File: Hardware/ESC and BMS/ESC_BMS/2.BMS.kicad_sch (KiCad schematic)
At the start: 37 parts, among them Q301 SQJ141ELP, Q302 SQJ141ELP, Q303 SQJ141ELP, Q304 SQJ412EP, Q305 SQJ141ELP, SW301 SW_SPST, U301 BQ2057W, U302 BQ2969T

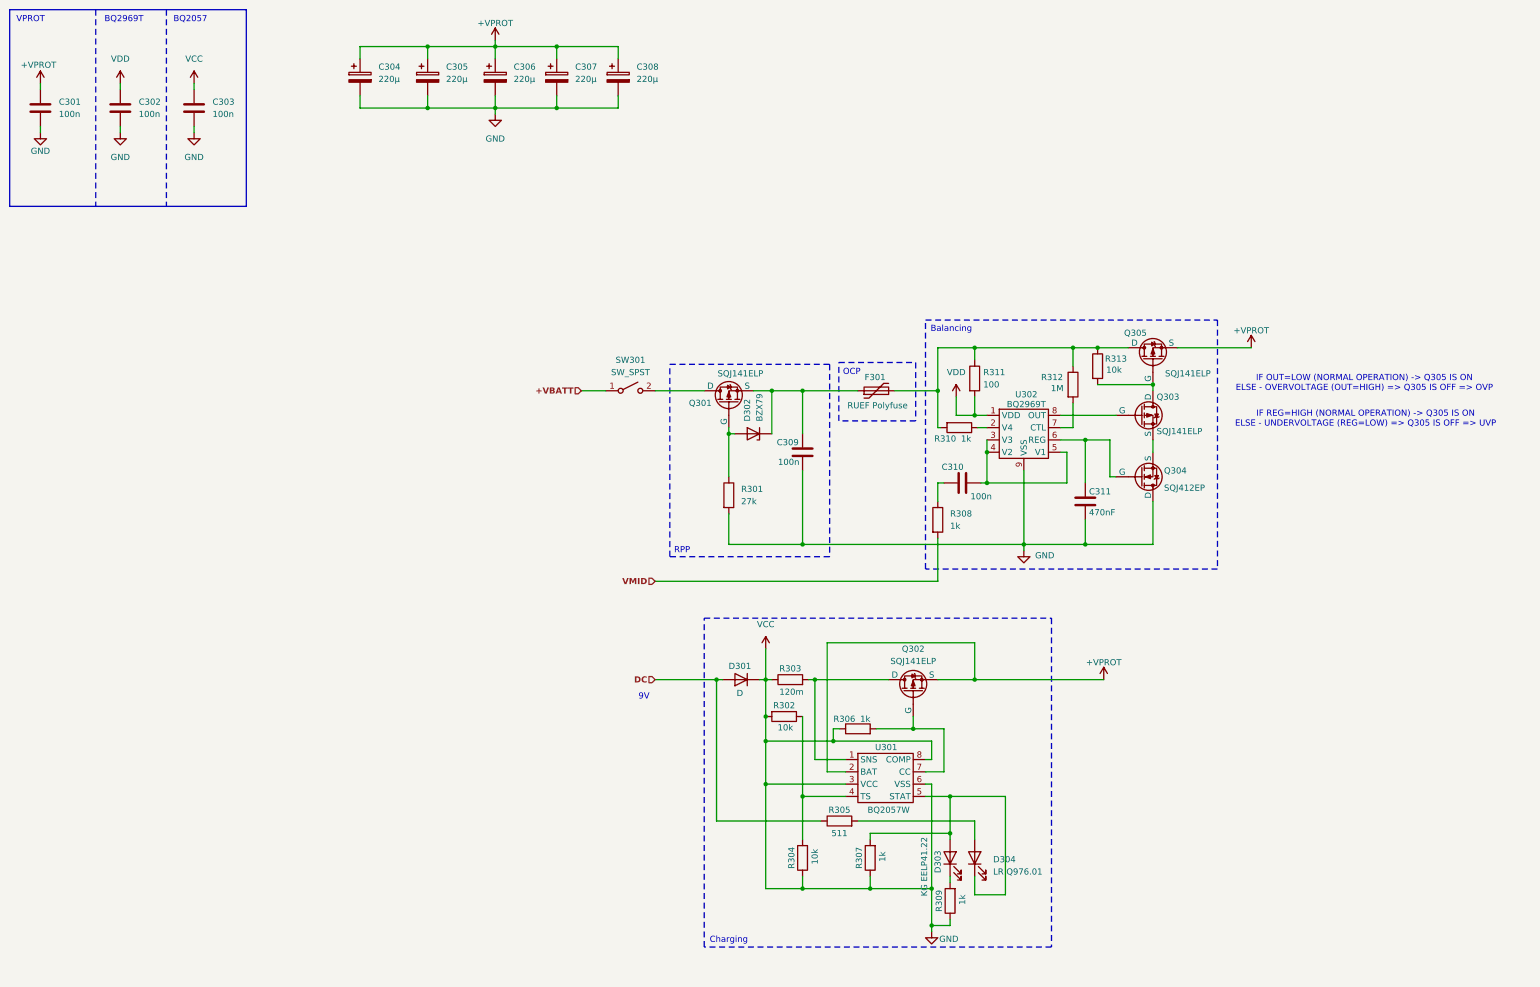
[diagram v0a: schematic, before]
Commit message: footprints almost done and LEDs for charger fixed
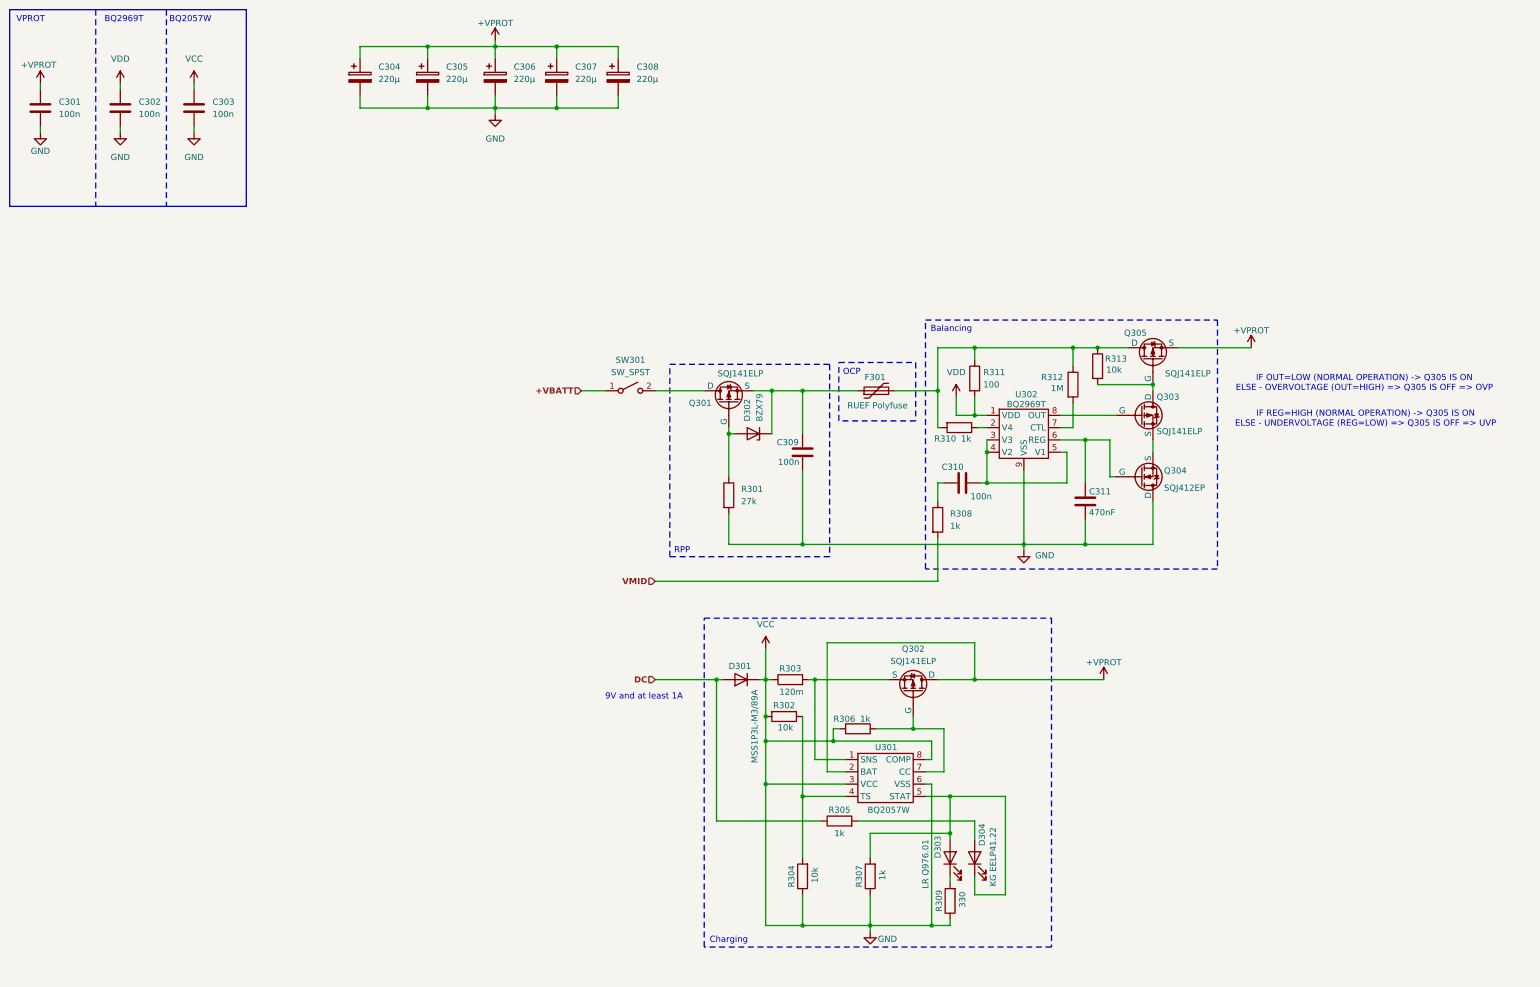
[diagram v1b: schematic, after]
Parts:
- D301: value D -> MSS1P3L-M3/89A
- D303: renamed from D304; footprint https://docs.rs-online.com/01aa/A700000010723894.pdf -> Diode_SMD:D_0603_1608Metric_Pad1.05x0.95mm_HandSolder
- D304: renamed from D303; footprint https://docs.rs-online.com/e1fe/A700000013302439.pdf -> Diode_SMD:D_0603_1608Metric_Pad1.05x0.95mm_HandSolder
- R305: value 511 -> 1k; footprint (none) -> Resistor_SMD:R_0603_1608Metric
- R306, R307, R308, R310, R311: footprint (none) -> Resistor_SMD:R_0603_1608Metric
- R309: value 1k -> 330; footprint (none) -> Resistor_SMD:R_0603_1608Metric
- R312: footprint (none) -> Resistor_SMD:R_0805_2012Metric_Pad1.20x1.40mm_HandSolder
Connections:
- net +VPROT: now also Q302.1 (D); no longer Q302.3 (S)
- net at R309.2: now also D303.1 (K); no longer D304.1 (K)
- net at R307.2, U301.5 (STAT): now also D303.2 (A), D304.1 (K); no longer D303.1 (K), D304.2 (A)
- net at R305.2: now also D304.2 (A); no longer D303.2 (A)
- net at R303.2, U301.1 (SNS): now also Q302.3 (S); no longer Q302.1 (D)
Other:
- note added: "9V and at least 1A"
- note added: "BQ2057W"
- note removed: "9V"
- note removed: "BQ2057"
- moved on the sheet: D303, D304, Q302, R304, R307

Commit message: ESC/BMS fully ready for PCB
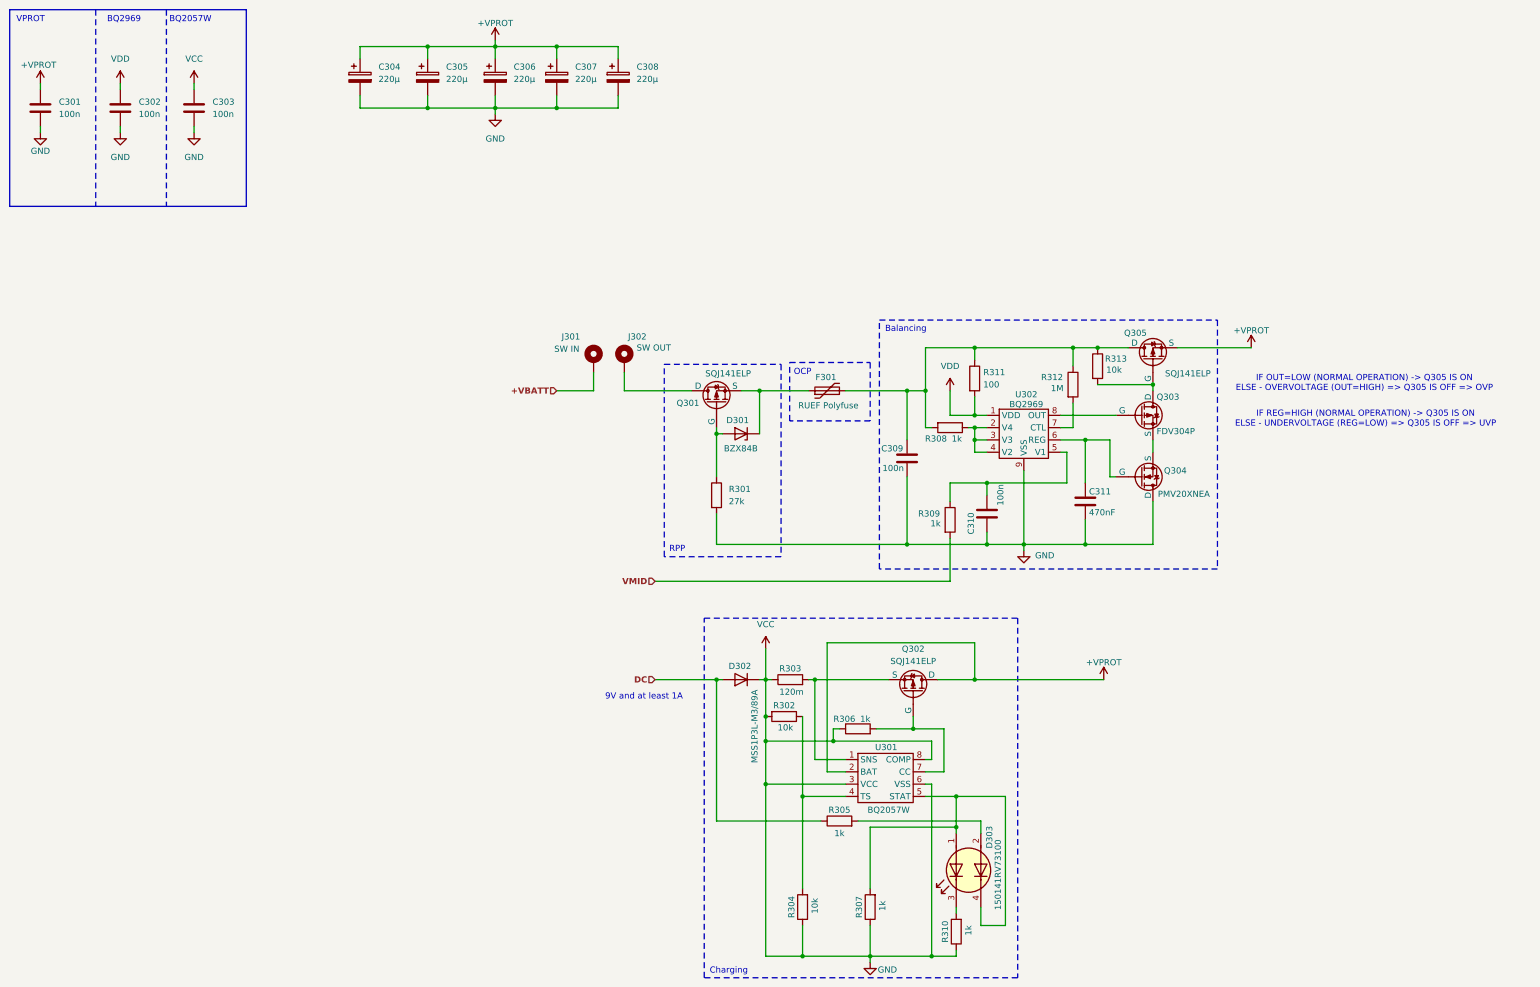
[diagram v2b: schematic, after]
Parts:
- removed D303: LR Q976.01, Diode_SMD:D_0603_1608Metric_Pad1.05x0.95mm_HandSolder, symbol Device:LED
- removed D304: KG EELP41.22, Diode_SMD:D_0603_1608Metric_Pad1.05x0.95mm_HandSolder, symbol Device:LED
- removed SW301: SW_SPST, symbol Switch:SW_SPST
- added D303: 150141RV73100, LED_SMD:LED_RGB_Wuerth-PLCC4_3.2x2.8mm_150141M173100, symbol Device:LED_Dual_AAKK
- added J301: SW IN, Connector_Wire:SolderWire-1sqmm_1x01_D1.4mm_OD2.7mm, symbol Mechanical:MountingHole_Pad
- added J302: SW OUT, Connector_Wire:SolderWire-1sqmm_1x01_D1.4mm_OD2.7mm, symbol Mechanical:MountingHole_Pad
- C311: footprint Capacitor_SMD:C_1206_3216Metric_Pad1.33x1.80mm_HandSolder -> Capacitor_SMD:C_0603_1608Metric_Pad1.08x0.95mm_HandSolder
- D301: renamed from D302; value BZX79 -> BZX84B; footprint Diode_THT:D_DO-35_SOD27_P10.16mm_Horizontal -> Package_TO_SOT_SMD:SOT-23
- Q303: value SQJ141ELP -> FDV304P; footprint Package_SO:PowerPAK_SO-8L_Single -> Package_TO_SOT_SMD:SOT-23
- Q304: value SQJ412EP -> PMV20XNEA; footprint Package_SO:PowerPAK_SO-8L_Single -> Package_TO_SOT_SMD:SOT-23
- R310: renamed from R309; value 330 -> 1k
- U302: value BQ2969T -> BQ2969; footprint (none) -> Package_SON:WSON-8-1EP_3x3mm_P0.5mm_EP1.2x2mm_ThermalVias
- renumbered D301 to D302, R310 to R308, R308 to R309
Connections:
- net +VBATT: now also J301.1
- net GND: now also C310.1
- net at R310.2: now also D303.3 (K1)
- net at F301.2, Q305.1 (D), R308.2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: now also C309.1
- net at D301.1 (K), F301.1, Q301.3 (S): no longer C309.1
- net at Q301.1 (D): now also J302.1
- net at R307.2, U301.5 (STAT): now also D303.1 (A1), D303.4 (K2)
- net at R309.1: now also C310.2, U302.5 (V1); no longer C310.1
- net at U302.3 (V3), U302.4 (V2): now also R308.1, U302.2 (V4); no longer C310.2, U302.5 (V1)
- net at R305.2: now also D303.2 (A2)
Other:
- note added: "BQ2969"
- note removed: "BQ2969T"
- moved on the sheet: C309, C310, D301, F301, Q301, R301, R304, R307, R308, R309, R310

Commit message: PCB component placement init
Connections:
- net GND: no longer C303.1
- net DC renamed VCC
- net VCC: now also C303.1
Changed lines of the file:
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@@
-	(wire
-		(pts
-			(xy 172.72 148.59) (xy 172.72 154.94)
-		)
-		(stroke
-			(width 0)
-			(type default)
-		)
-	)
 	(wire
 		(pts
@@
 		(pts
 			(xy 181.61 154.94) (xy 182.88 154.94)
+		)
+		(stroke
+			(width 0)
+			(type default)
+		)
+	)
+	(wire
+		(pts
+			(xy 162.56 151.13) (xy 162.56 154.94)
 		)
 		(stroke
@@
 	(symbol
 		(lib_id "power:+3.3V")
-		(at 172.72 148.59 0)
+		(at 162.56 151.13 0)
 		(unit 1)
 		(exclude_from_sim no)
@@
 		(fields_autoplaced yes)
 		(property "Reference" "#PWR0309"
-			(at 172.72 152.4 0)
+			(at 162.56 154.94 0)
 			(effects
 				(font
@@
 		)
 		(property "Value" "VCC"
-			(at 172.72 143.51 0)
+			(at 162.56 146.05 0)
 			(effects
 				(font
@@
 		)
 		(property "Footprint" ""
-			(at 172.72 148.59 0)
+			(at 162.56 151.13 0)
 			(effects
 				(font
@@
 		)
 		(property "Datasheet" ""
-			(at 172.72 148.59 0)
+			(at 162.56 151.13 0)
 			(effects
 				(font
@@
 		)
 		(property "Description" "Power symbol creates a global label with name \"+3.3V\""
-			(at 172.72 148.59 0)
+			(at 162.56 151.13 0)
 			(effects
 				(font
@@
 		(dnp no)
 		(fields_autoplaced yes)
-		(property "Reference" "#PWR0305"
+		(property "Reference" "#PWR0101"
 			(at 54.61 35.56 0)
 			(effects
@@
 			(project "SPROJ3EE_ESC_BMS"
 				(path "/64aee9f2-a448-43ef-b28d-f00e276bd9f5/eb2740b7-11f5-4644-9e72-e71a449b99af"
-					(reference "#PWR0305")
+					(reference "#PWR0101")
 					(unit 1)
 				)

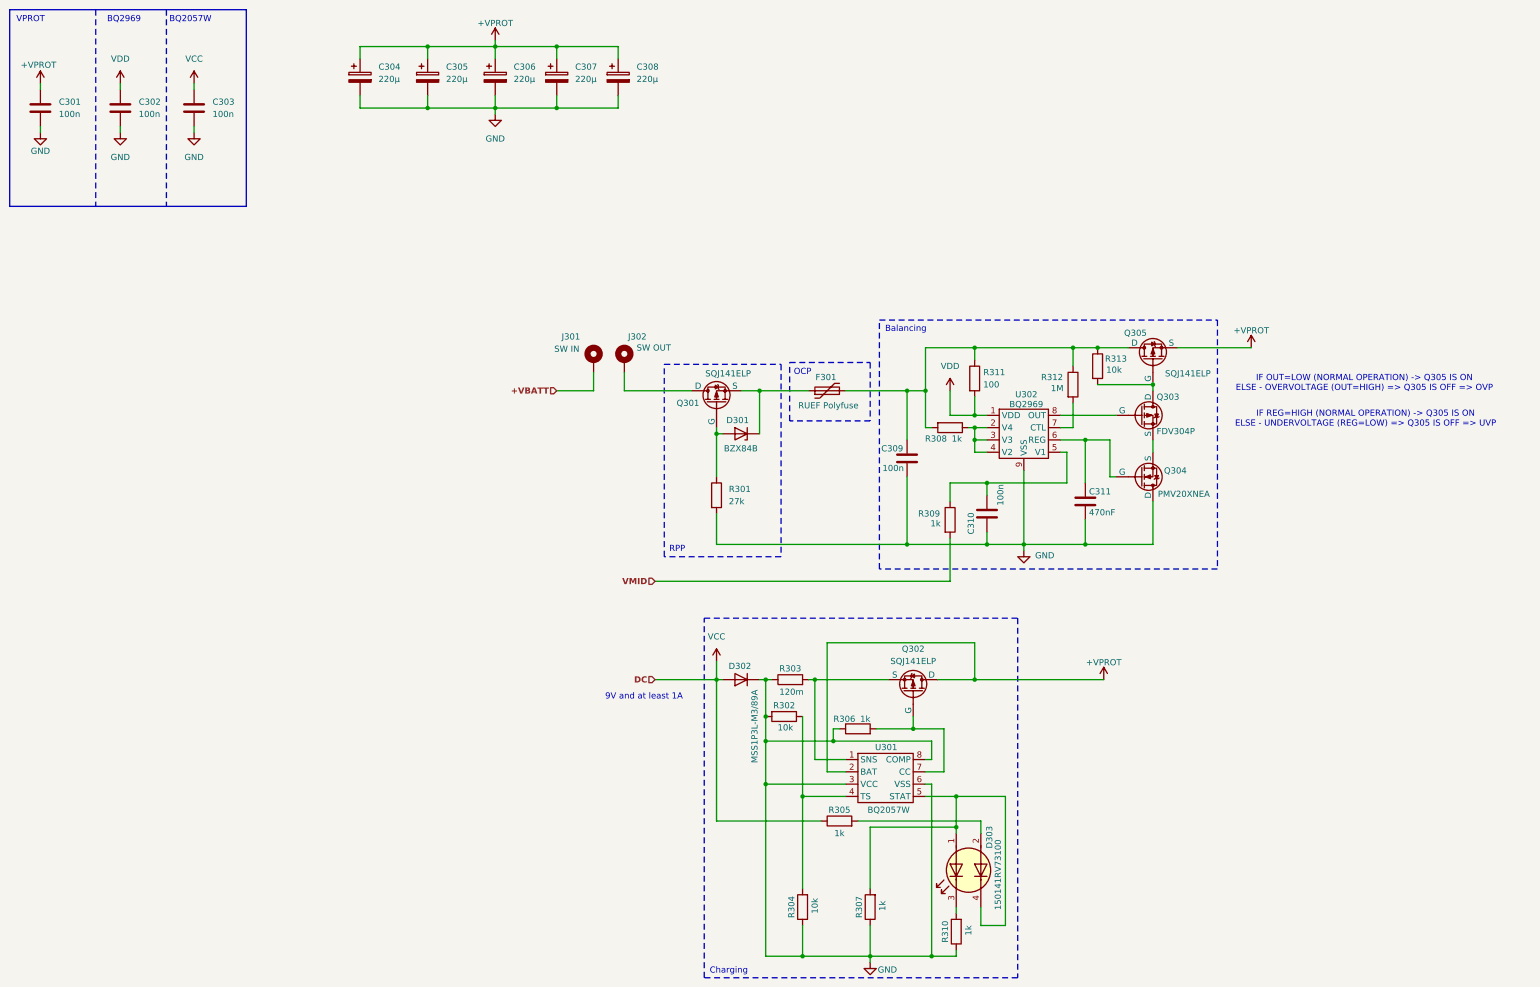
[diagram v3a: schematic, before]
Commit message: ESC BMS component placement close to done
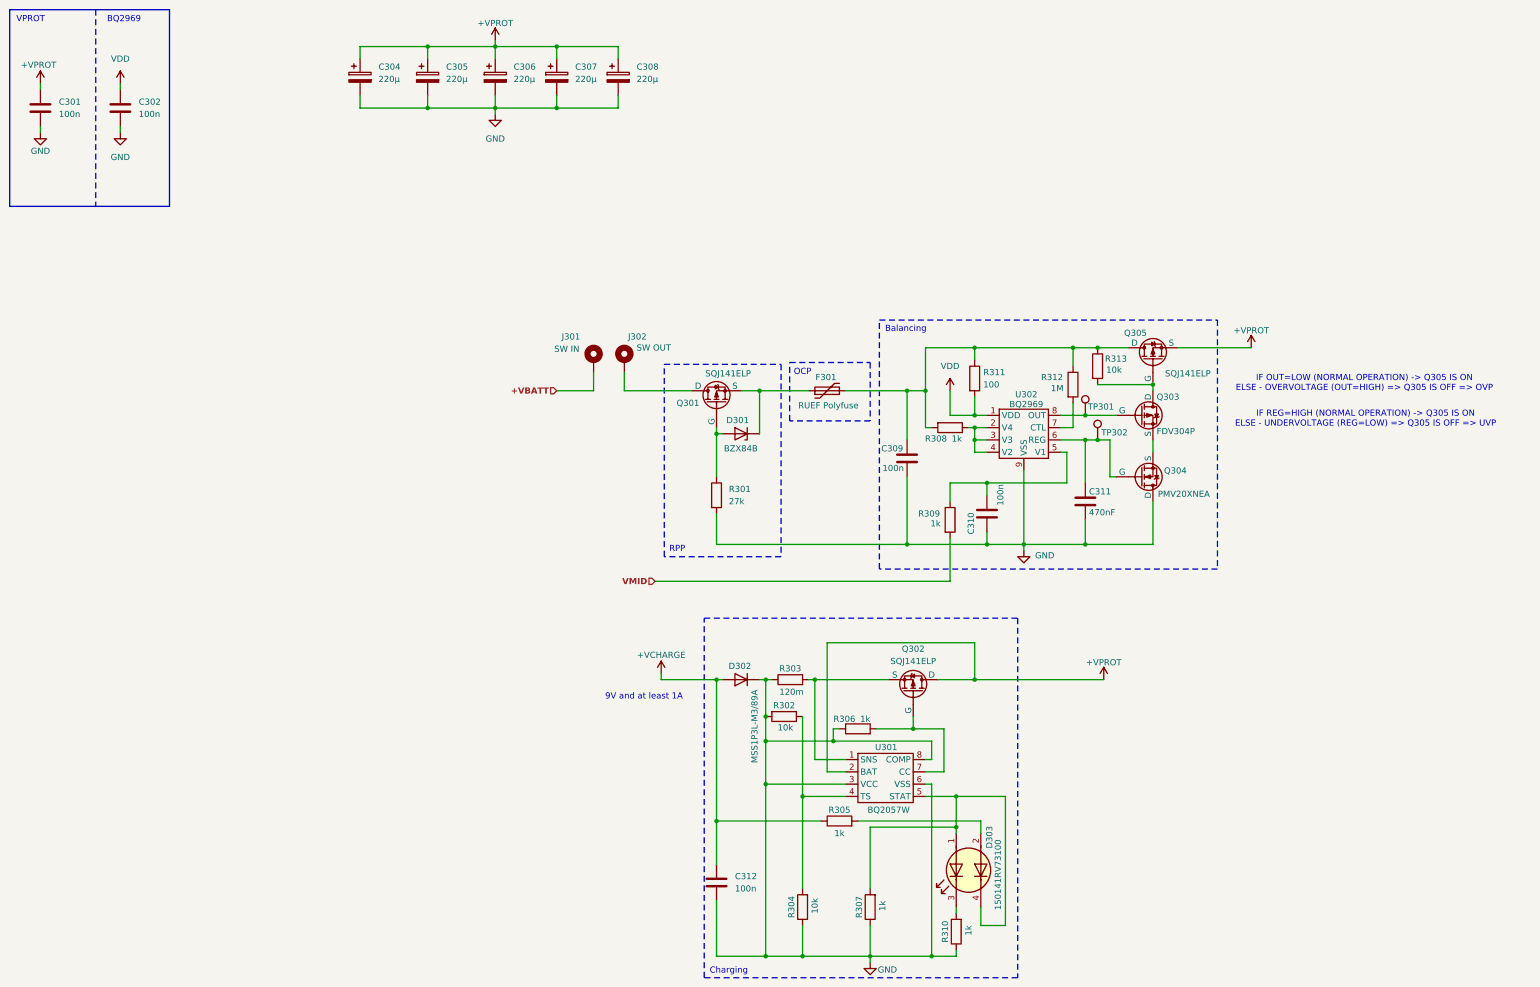
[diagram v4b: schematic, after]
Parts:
- removed C303: 100n, Capacitor_SMD:C_0805_2012Metric_Pad1.18x1.45mm_HandSolder, symbol Device:C
- added C312: 100n, Capacitor_SMD:C_0805_2012Metric_Pad1.18x1.45mm_HandSolder, symbol Device:C
- added TP301, TP302: TestPoint, TestPoint:TestPoint_Pad_D1.0mm, symbol Connector:TestPoint
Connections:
- net GND: now also C312.2
- net at C311.1, Q304.2 (G), U302.6 (REG): now also TP302.1
- net at Q303.2 (G), U302.8 (OUT): now also TP301.1
- net VCC renamed +VCHARGE
- net +VCHARGE: now also C312.1
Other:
- note removed: "BQ2057W"
